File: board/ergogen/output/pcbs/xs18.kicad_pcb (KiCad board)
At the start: 2 copper layers, 220.5 x 102.5 mm, 18 parts

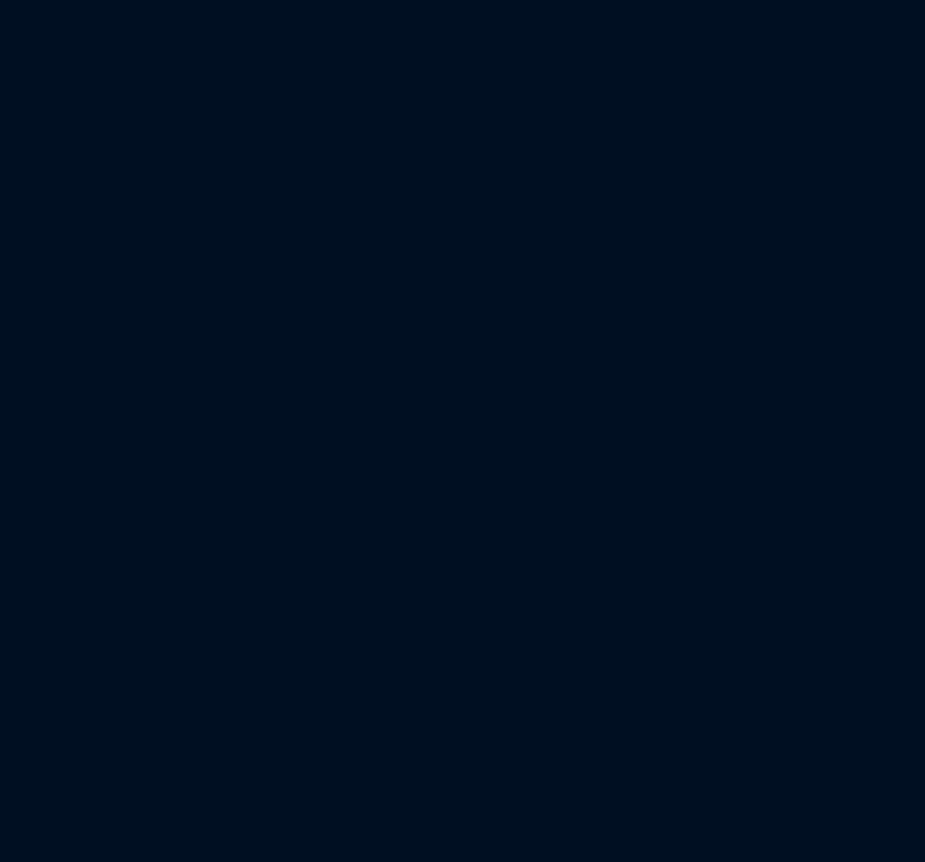
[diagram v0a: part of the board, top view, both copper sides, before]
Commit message: feat: add xiao to PCB
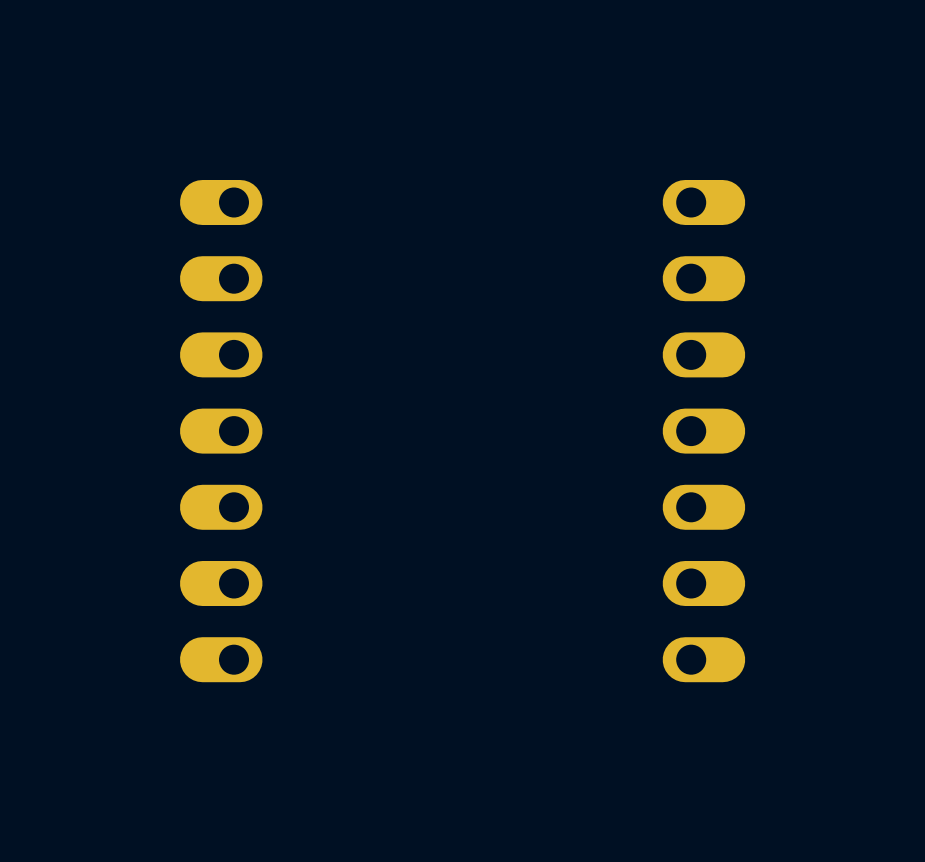
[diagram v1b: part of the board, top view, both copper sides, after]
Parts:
- added MCU1: , xiao-ble, F.Cu at (219.5, 186.4)
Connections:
- S1 pad 2: P7 -> P0
- S10 pad 2: P7 -> P2
- S11 pad 2: P0 -> P7
- S12 pad 2: P0 -> P7
- S13 pad 2: P1 -> P0
- S14 pad 2: P1 -> P0
- S16 pad 2: P1 -> P7
- S17 pad 2: P0 -> P1
- S18 pad 2: P1 -> P2
- S4 pad 2: P0 -> P2
- S5 pad 2: P0 -> P2
- S8 pad 2: P7 -> P1
- S9 pad 2: P7 -> P2

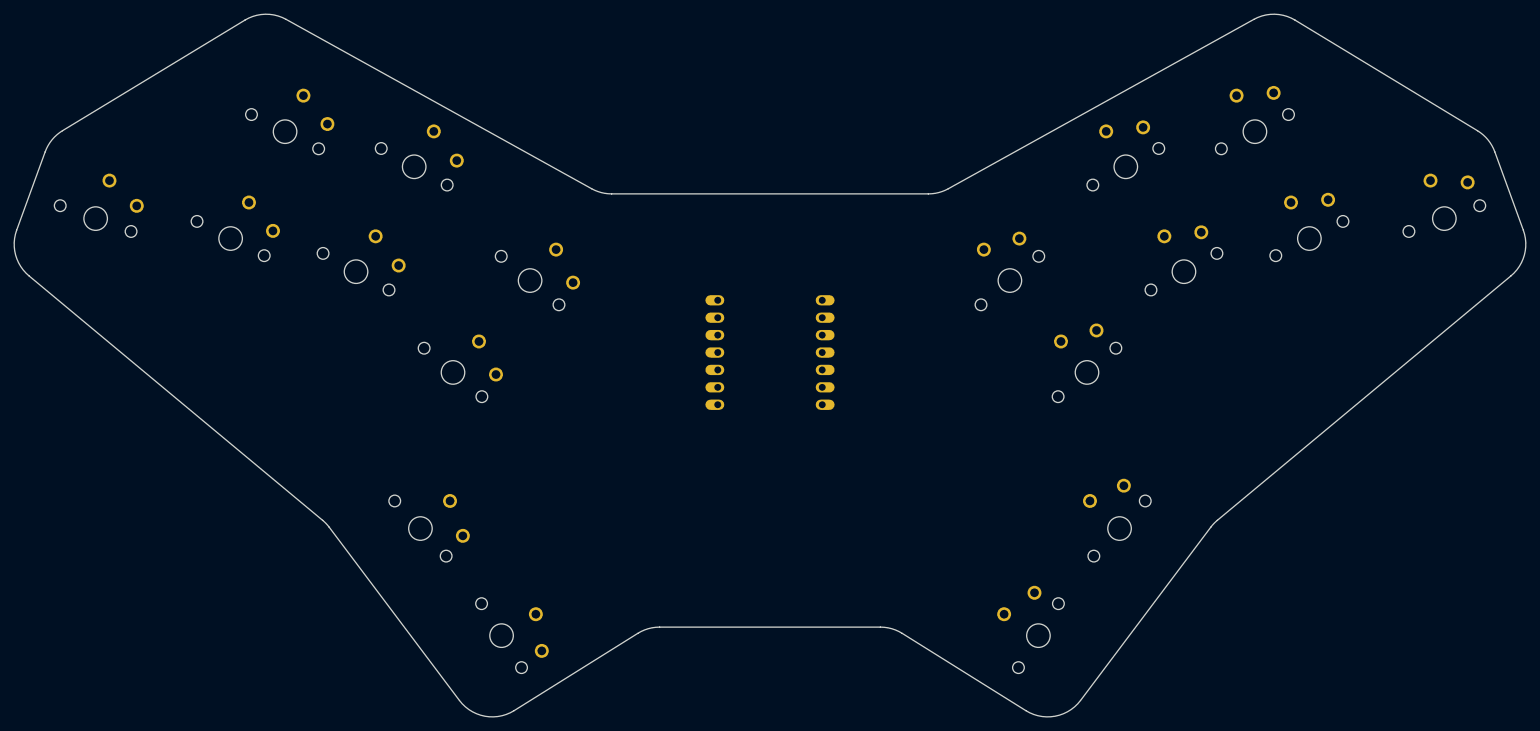
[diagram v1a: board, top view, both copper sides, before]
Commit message: feat: add diodes to PCB
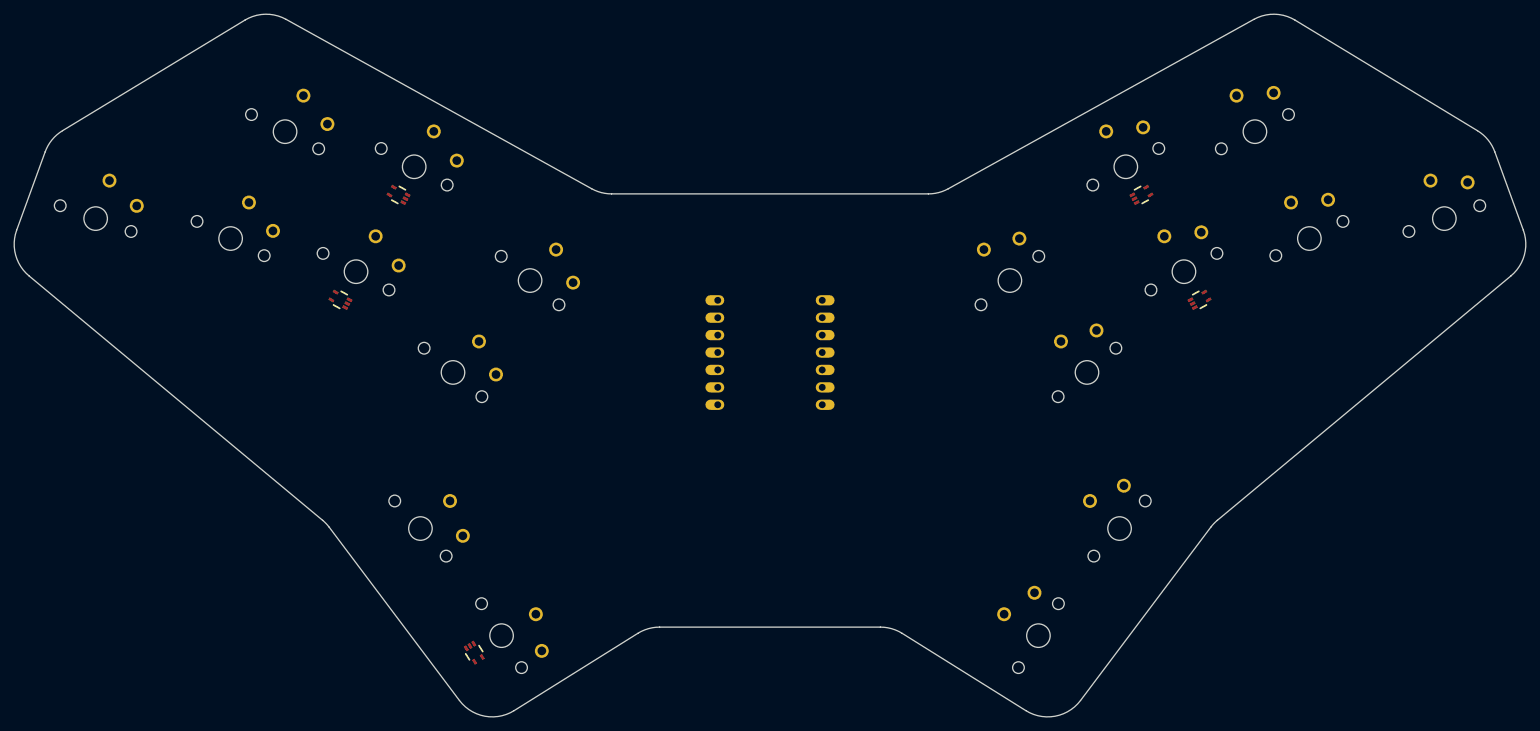
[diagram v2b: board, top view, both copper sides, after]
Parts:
- added D1: UMP1NTR, easyeda2kicad:SOT-353_L2.1-W1.3-P0.65-LS2.3-BL, F.Cu at (156.8, 178.7)
- added D2: UMP1NTR, easyeda2kicad:SOT-353_L2.1-W1.3-P0.65-LS2.3-BL, F.Cu at (165.3, 163.4)
- added D3: UMP1NTR, easyeda2kicad:SOT-353_L2.1-W1.3-P0.65-LS2.3-BL, F.Cu at (282.1, 178.7)
- added D4: UMP1NTR, easyeda2kicad:SOT-353_L2.1-W1.3-P0.65-LS2.3-BL, F.Cu at (273.6, 163.4)
- added D5: UMP1NTR, easyeda2kicad:SOT-353_L2.1-W1.3-P0.65-LS2.3-BL, F.Cu at (176.3, 230.2)
